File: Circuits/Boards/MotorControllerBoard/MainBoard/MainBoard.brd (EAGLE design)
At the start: 160 x 100 mm, 56 parts, among them IC2 788TV, M1 IRFS7537PBF, M2 IRFS7537PBF, M3 IRFS7537PBF, M4 IRFS7537PBF, Q1 2N3904, Q2 2N3904, Q3 2N3904, Q4 2N3904, Q5 2N3904, Q6 2N3904, Q7 2N3904, Q8 2N3904

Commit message: Finished board files and updated gitignore
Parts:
- added PAD8, PAD9: WIREPAD2,54/1,1, wirepad:2,54/1,1
- PAD2: value WIREPAD4,16O1,6 -> (none); device wirepad:4,16O1,6 -> wirepad:3,81/1,4
- PAD4: value (none) -> WIREPAD4,16O1,6; device wirepad:2,54/1,0 -> wirepad:4,16O1,6
- PAD6: device wirepad:3,81/1,4 -> wirepad:2,54/1,0
- moved PAD4 115.0 mm to (119.4, 45.7)
- moved PAD6 104.8 mm to (6.35, 39.4)
- moved PAD1 76.2 mm to (88.9, 95.2)
- moved PAD5 73.7 mm to (88.9, 19.1)
- moved PAD2 48.4 mm to (95.2, 95.2)
- moved C2 17.8 mm to (27.9, 64.8), turned to 180 degrees
- moved D5 11.7 mm to (25.4, 27.9), turned to 0 degrees
- moved Q1 11.5 mm to (33.0, 36.8)
- moved R2 10.2 mm to (12.7, 55.9)
- moved Q3 10.2 mm to (49.5, 44.5)
- moved R5 10.2 mm to (39.4, 44.5)
- moved R14 9.92 mm to (20.3, 68.6), turned to 0 degrees
- moved R1 9.16 mm to (24.1, 34.3), turned to 0 degrees
- moved R11 7.73 mm to (14.0, 44.5)
- moved R3 7.73 mm to (17.8, 53.3)
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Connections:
- new net FBJ: PAD9.1, Q7.2
- net FB: now also PAD8.1; no longer Q7.2
- net MN: now also PAD4.1; no longer PAD3.1
- net MP: now also PAD3.1; no longer PAD2.1
- net N$1: now also PAD2.1; no longer PAD6.1
- net PWM: now also PAD6.1; no longer PAD4.1
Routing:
- net VDD: track 298.1 -> 454.3 mm
- net N$16: track 69.8 -> 156.2 mm
- net 0: track 595.9 -> 556.8 mm
- net FB: track 84.5 -> 56.7 mm
- net DIR: track 16.5 -> 34.3 mm
- net FBJ: track 0.00 -> 15.6 mm
- net BB: track 77.5 -> 62.2 mm
- net VSW: track 148.4 -> 138.2 mm
- net VG2: track 55.9 -> 66.0 mm
- net BF: track 80.0 -> 69.9 mm
- net MP: track 76.7 -> 71.6 mm
- net N$20: track 89.5 -> 94.1 mm
- net N$1: track 67.0 -> 71.2 mm
- net N$27: track 45.7 -> 49.5 mm
- net FF: track 119.4 -> 115.6 mm
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
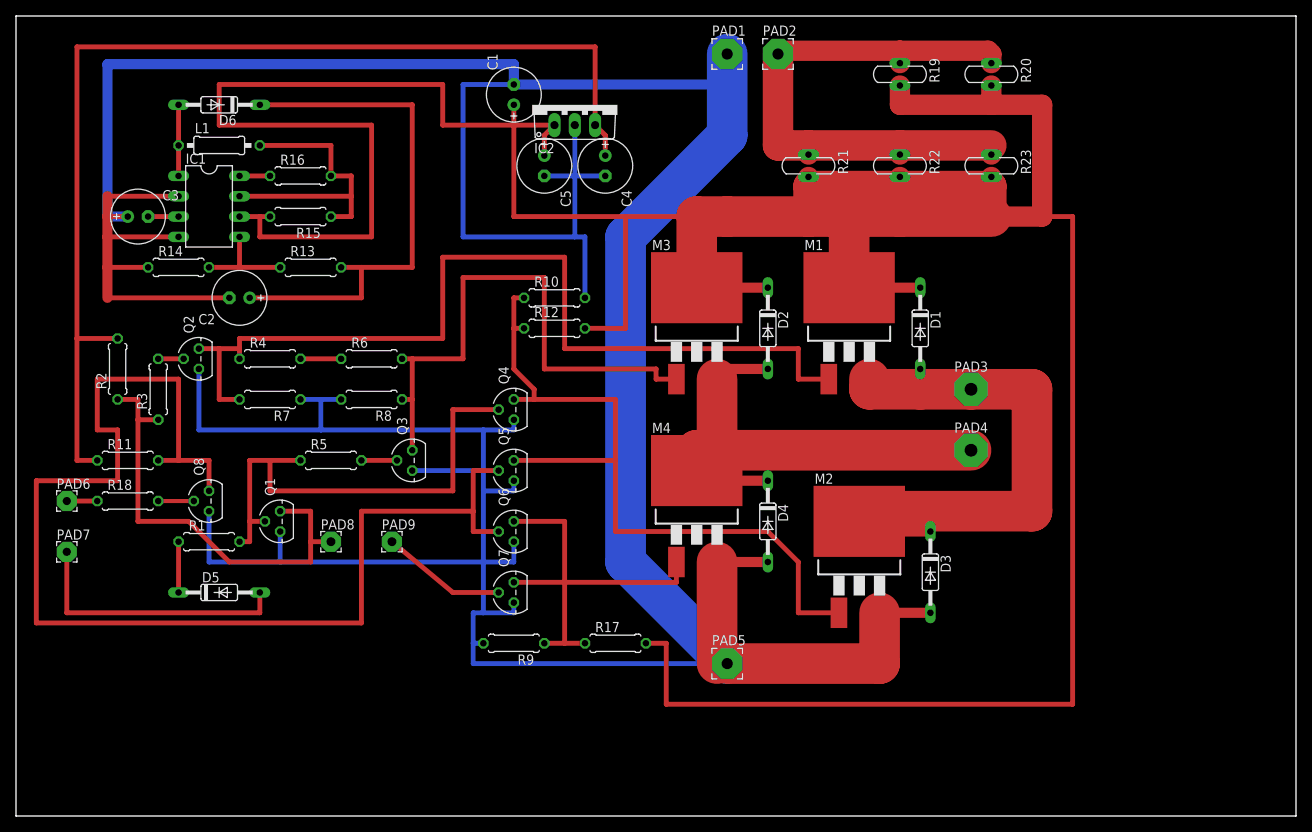
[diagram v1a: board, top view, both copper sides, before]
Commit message: Fixed board CNC errors, ready for cutting on othermill
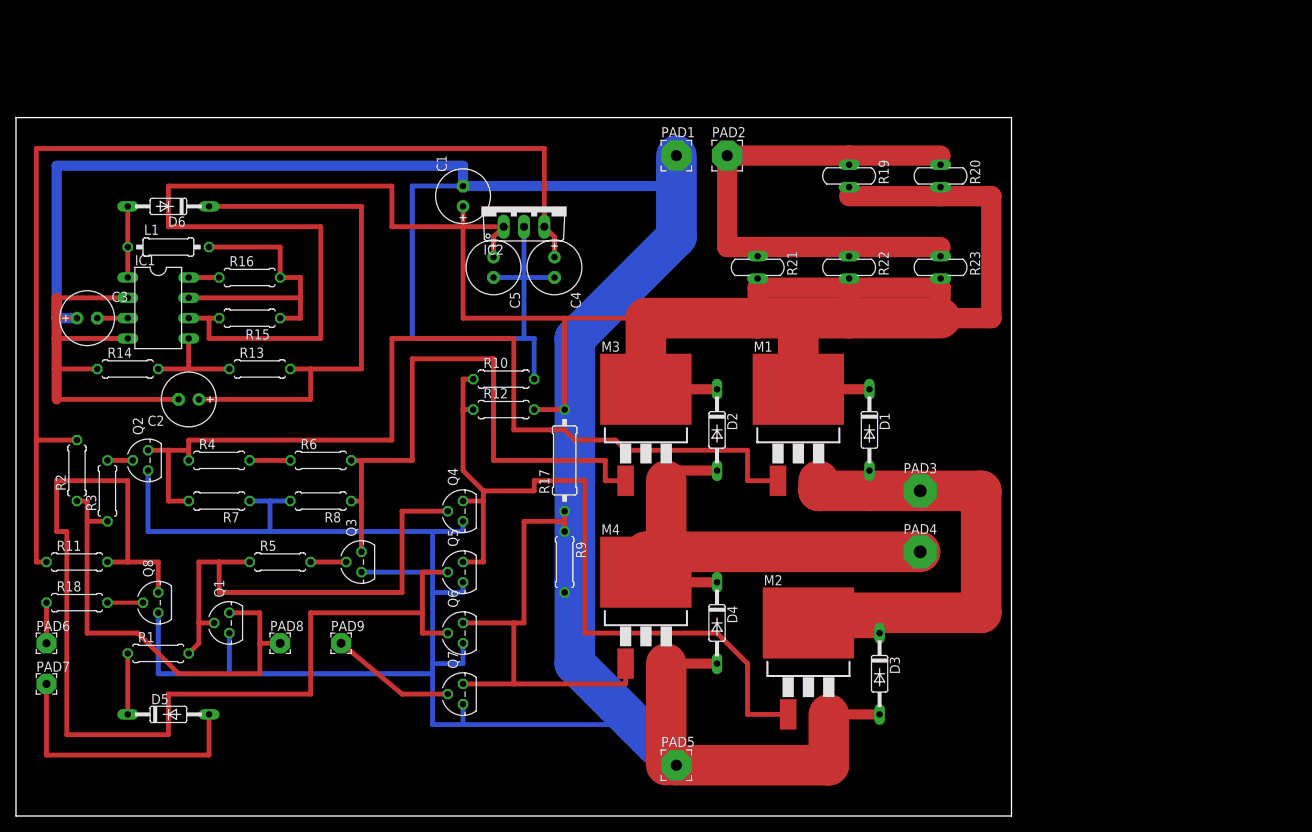
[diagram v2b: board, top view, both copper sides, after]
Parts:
- R17: device rcl:0207/7 -> resistor:0309/12
- moved R17 23.7 mm to (68.6, 44.5), turned to 90 degrees
- moved PAD6 18.0 mm to (3.81, 21.6)
- moved PAD7 16.7 mm to (3.81, 16.5)
- moved D5 16.5 mm to (19.1, 12.7)
- moved R1 15.3 mm to (17.8, 20.3)
- moved C3 14.2 mm to (8.89, 62.2)
- moved R15 14.2 mm to (29.2, 62.2)
- moved C5 14.2 mm to (59.7, 68.6)
- moved D2 14.2 mm to (87.6, 48.3)
- moved M3 14.2 mm to (78.7, 50.8)
- moved PAD1 14.2 mm to (82.5, 82.5)
- moved R21 14.2 mm to (92.7, 68.6)
- moved R23 14.2 mm to (115.6, 68.6)
- moved PAD5 14.2 mm to (82.5, 6.35)
- moved Q3 14.2 mm to (43.2, 31.8)
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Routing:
- net VDD: track 454.3 -> 323.5 mm
- net N$16: track 156.2 -> 135.9 mm
- net 0: track 556.8 -> 542.1 mm
- net N$27: track 49.5 -> 58.4 mm
- net BF: track 69.9 -> 74.9 mm
- net N$20: track 94.1 -> 97.9 mm
- net FF: track 115.6 -> 119.2 mm
- net VSW: track 138.2 -> 135.7 mm
- net N$19: track 6.35 -> 7.62 mm
- net FB: track 56.7 -> 58.0 mm
- net PWM: track 3.81 -> 5.08 mm
- net BB: track 62.2 -> 62.8 mm
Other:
- board size 160 x 100 mm -> 124.4 x 87.3 mm

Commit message: Minor updates to Motor Controller
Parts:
- added D7: 1N4148DO35-10, diode:DO35-10
- moved PAD6 10.2 mm to (3.81, 11.4)
- moved PAD7 8.89 mm to (3.81, 7.62), turned to 90 degrees
- moved R18 2.54 mm to (7.62, 29.2)
- moved R11 1.27 mm to (7.62, 33.0)
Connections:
- removed net PWM: PAD6.1, R18.1
- new net N$2: D7.C, R18.1
- new net N$4: D7.A, PAD6.1
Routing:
- net DIR: track 34.3 -> 25.4 mm
- net PWM: track 5.08 -> 0.00 mm
- net N$2: track 0.00 -> 3.81 mm
- net N$4: track 0.00 -> 3.81 mm
- net N$23: track 4.45 -> 6.98 mm
- net VSW: track 135.7 -> 134.4 mm
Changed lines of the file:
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@@
 <attribute name="SPICEPREFIX" value="R" x="60.96" y="54.61" size="1.778" layer="27" display="off"/>
 </element>
-<element name="R11" library="rcl" library_urn="urn:adsk.eagle:library:334" package="0207/7" package3d_urn="urn:adsk.eagle:package:23493/1" value="" x="7.62" y="31.75">
-<attribute name="SPICEPREFIX" value="R" x="7.62" y="31.75" size="1.778" layer="27" display="off"/>
+<element name="R11" library="rcl" library_urn="urn:adsk.eagle:library:334" package="0207/7" package3d_urn="urn:adsk.eagle:package:23493/1" value="" x="7.62" y="33.02">
+<attribute name="SPICEPREFIX" value="R" x="7.62" y="33.02" size="1.778" layer="27" display="off"/>
 </element>
 <element name="R12" library="rcl" library_urn="urn:adsk.eagle:library:334" package="0207/7" package3d_urn="urn:adsk.eagle:package:23493/1" value="" x="60.96" y="50.8">
@@
 </element>
 <element name="R17" library="resistor" library_urn="urn:adsk.eagle:library:348" package="0309/12" package3d_urn="urn:adsk.eagle:package:26089/1" value="" x="68.58" y="44.45" rot="R90"/>
-<element name="R18" library="rcl" library_urn="urn:adsk.eagle:library:334" package="0207/7" package3d_urn="urn:adsk.eagle:package:23493/1" value="" x="7.62" y="26.67">
-<attribute name="SPICEPREFIX" value="R" x="7.62" y="26.67" size="1.778" layer="27" display="off"/>
+<element name="R18" library="rcl" library_urn="urn:adsk.eagle:library:334" package="0207/7" package3d_urn="urn:adsk.eagle:package:23493/1" value="" x="7.62" y="29.21">
+<attribute name="SPICEPREFIX" value="R" x="7.62" y="29.21" size="1.778" layer="27" display="off"/>
 </element>
 <element name="C1" library="rcl" library_urn="urn:adsk.eagle:library:334" package="E2,5-7" package3d_urn="urn:adsk.eagle:package:23345/1" value="" x="55.88" y="77.47" rot="R90">
@@
 <element name="PAD3" library="wirepad" library_urn="urn:adsk.eagle:library:412" package="4,16O1,6" package3d_urn="urn:adsk.eagle:package:30843/1" value="WIREPAD4,16O1,6" x="113.03" y="40.64"/>
 <element name="PAD4" library="wirepad" library_urn="urn:adsk.eagle:library:412" package="4,16O1,6" package3d_urn="urn:adsk.eagle:package:30843/1" value="WIREPAD4,16O1,6" x="113.03" y="33.02"/>
-<element name="PAD6" library="wirepad" library_urn="urn:adsk.eagle:library:412" package="2,54/1,0" package3d_urn="urn:adsk.eagle:package:30828/1" value="" x="3.81" y="21.59"/>
+<element name="PAD6" library="wirepad" library_urn="urn:adsk.eagle:library:412" package="2,54/1,0" package3d_urn="urn:adsk.eagle:package:30828/1" value="" x="3.81" y="11.43"/>
 <element name="PAD1" library="wirepad" library_urn="urn:adsk.eagle:library:412" package="3,81/1,4" package3d_urn="urn:adsk.eagle:package:30835/1" value="" x="82.55" y="82.55"/>
 <element name="PAD2" library="wirepad" library_urn="urn:adsk.eagle:library:412" package="3,81/1,4" package3d_urn="urn:adsk.eagle:package:30835/1" value="" x="88.9" y="82.55"/>
-<element name="PAD7" library="wirepad" library_urn="urn:adsk.eagle:library:412" package="2,54/1,0" package3d_urn="urn:adsk.eagle:package:30828/1" value="" x="3.81" y="16.51"/>
+<element name="PAD7" library="wirepad" library_urn="urn:adsk.eagle:library:412" package="2,54/1,0" package3d_urn="urn:adsk.eagle:package:30828/1" value="" x="3.81" y="7.62" rot="R90"/>
 <element name="R19" library="ptc-ntc" library_urn="urn:adsk.eagle:library:332" package="P660A" package3d_urn="urn:adsk.eagle:package:22777/1" value="" x="104.14" y="80.01" rot="R270">
 <attribute name="MF" value="" x="104.14" y="80.01" size="1.778" layer="27" rot="R270" display="off"/>
@@
 <element name="PAD8" library="wirepad" library_urn="urn:adsk.eagle:library:412" package="2,54/1,1" package3d_urn="urn:adsk.eagle:package:30836/1" value="WIREPAD2,54/1,1" x="33.02" y="21.59"/>
 <element name="PAD9" library="wirepad" library_urn="urn:adsk.eagle:library:412" package="2,54/1,1" package3d_urn="urn:adsk.eagle:package:30836/1" value="WIREPAD2,54/1,1" x="40.64" y="21.59"/>
+<element name="D7" library="diode" library_urn="urn:adsk.eagle:library:210" package="DO35-10" package3d_urn="urn:adsk.eagle:package:43344/2" value="1N4148DO35-10" x="3.81" y="20.32" rot="R270"/>
 </elements>
 <signals>
@@
 <contactref element="Q6" pad="2"/>
 <contactref element="R11" pad="2"/>
-<wire x1="11.43" y1="31.75" x2="13.97" y2="31.75" width="0.6096" layer="1"/>
-<wire x1="13.97" y1="31.75" x2="17.78" y2="31.75" width="0.6096" layer="1"/>
-<wire x1="17.78" y1="31.75" x2="17.78" y2="27.94" width="0.6096" layer="1"/>
+<wire x1="11.43" y1="33.02" x2="13.97" y2="33.02" width="0.6096" layer="1"/>
+<wire x1="13.97" y1="33.02" x2="17.78" y2="33.02" width="0.6096" layer="1"/>
+<wire x1="17.78" y1="33.02" x2="17.78" y2="27.94" width="0.6096" layer="1"/>
 <wire x1="53.975" y1="30.48" x2="50.8" y2="30.48" width="0.6096" layer="1"/>
 <wire x1="50.8" y1="30.48" x2="50.8" y2="25.4" width="0.6096" layer="1"/>
 <wire x1="50.8" y1="25.4" x2="50.8" y2="22.86" width="0.6096" layer="1"/>
 <wire x1="50.8" y1="22.86" x2="53.975" y2="22.86" width="0.6096" layer="1"/>
-<wire x1="13.97" y1="31.75" x2="13.97" y2="41.91" width="0.6096" layer="1"/>
+<wire x1="13.97" y1="33.02" x2="13.97" y2="41.91" width="0.6096" layer="1"/>
 <wire x1="13.97" y1="41.91" x2="5.08" y2="41.91" width="0.6096" layer="1"/>
-<wire x1="5.08" y1="41.91" x2="5.08" y2="35.56" width="0.6096" layer="1"/>
-<wire x1="5.08" y1="35.56" x2="6.35" y2="35.56" width="0.6096" layer="1"/>
+<wire x1="5.08" y1="41.91" x2="5.08" y2="36.83" width="0.6096" layer="1"/>
+<wire x1="5.08" y1="36.83" x2="6.35" y2="36.83" width="0.6096" layer="1"/>
 <wire x1="36.83" y1="25.4" x2="50.8" y2="25.4" width="0.6096" layer="1"/>
 <wire x1="6.35" y1="10.16" x2="19.05" y2="10.16" width="0.6096" layer="1"/>
@@
 <wire x1="19.05" y1="15.24" x2="36.83" y2="15.24" width="0.6096" layer="1"/>
 <wire x1="36.83" y1="15.24" x2="36.83" y2="25.4" width="0.6096" layer="1"/>
-<wire x1="6.35" y1="35.56" x2="6.35" y2="10.16" width="0.6096" layer="1"/>
+<wire x1="6.35" y1="36.83" x2="6.35" y2="10.16" width="0.6096" layer="1"/>
 </signal>
 <signal name="MN">
@@
 <contactref element="Q8" pad="2"/>
 <contactref element="R18" pad="2"/>
-<wire x1="11.43" y1="26.67" x2="15.875" y2="26.67" width="0.508" layer="1"/>
+<wire x1="11.43" y1="29.21" x2="13.97" y2="29.21" width="0.6096" layer="1"/>
+<wire x1="13.97" y1="29.21" x2="13.97" y2="26.67" width="0.6096" layer="1"/>
+<wire x1="13.97" y1="26.67" x2="15.875" y2="26.67" width="0.6096" layer="1"/>
 </signal>
 <signal name="DIR">
 <contactref element="D5" pad="A"/>
 <contactref element="PAD7" pad="1"/>
-<wire x1="3.81" y1="16.51" x2="3.81" y2="7.62" width="0.6096" layer="1"/>
 <wire x1="3.81" y1="7.62" x2="24.13" y2="7.62" width="0.6096" layer="1"/>
 <wire x1="24.13" y1="7.62" x2="24.13" y2="12.7" width="0.6096" layer="1"/>
-</signal>
-<signal name="PWM">
-<contactref element="R18" pad="1"/>
-<contactref element="PAD6" pad="1"/>
-<wire x1="3.81" y1="26.67" x2="3.81" y2="21.59" width="0.6096" layer="1"/>
 </signal>
 <signal name="FB">
@@
 <wire x1="7.62" y1="46.99" x2="2.54" y2="46.99" width="0.6096" layer="1"/>
 <wire x1="2.54" y1="46.99" x2="2.54" y2="83.4392" width="0.6096" layer="1"/>
-<wire x1="2.54" y1="46.99" x2="2.54" y2="31.75" width="0.6096" layer="1"/>
-<wire x1="2.54" y1="31.75" x2="3.81" y2="31.75" width="0.6096" layer="1"/>
+<wire x1="2.54" y1="46.99" x2="2.54" y2="33.02" width="0.6096" layer="1"/>
+<wire x1="2.54" y1="33.02" x2="3.81" y2="33.02" width="0.6096" layer="1"/>
 </signal>
 <signal name="N$19">
@@
 <wire x1="48.26" y1="15.24" x2="53.975" y2="15.24" width="0.6096" layer="1"/>
 </signal>
+<signal name="N$2">
+<contactref element="R18" pad="1"/>
+<contactref element="D7" pad="C"/>
+<wire x1="3.81" y1="29.21" x2="3.81" y2="25.4" width="0.6096" layer="1"/>
+</signal>
+<signal name="N$4">
+<contactref element="D7" pad="A"/>
+<contactref element="PAD6" pad="1"/>
+<wire x1="3.81" y1="15.24" x2="3.81" y2="11.43" width="0.6096" layer="1"/>
+</signal>
 </signals>
